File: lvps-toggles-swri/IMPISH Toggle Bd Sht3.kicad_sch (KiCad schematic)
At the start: 66 parts, among them J3 BCS-110-L-D-TE, J4 BCS-110-L-D-TE, Q1 MMBT3904Q, Q10 MMBT3904Q, Q11 MMBT3906Q, Q12 ZXM61N02F, Q2 MMBT3906Q, Q3 ZXM61N02F, Q4 MMBT3904Q, Q5 MMBT3906Q, Q6 ZXM61N02F, Q7 MMBT3904Q, Q8 MMBT3906Q, Q9 ZXM61N02F, U1 BSP452, U2 AP22804AW5-7, U3 AP22804AW5-7, U4 BSP452, U5 AP22804AW5-7, U6 AP22804AW5-7

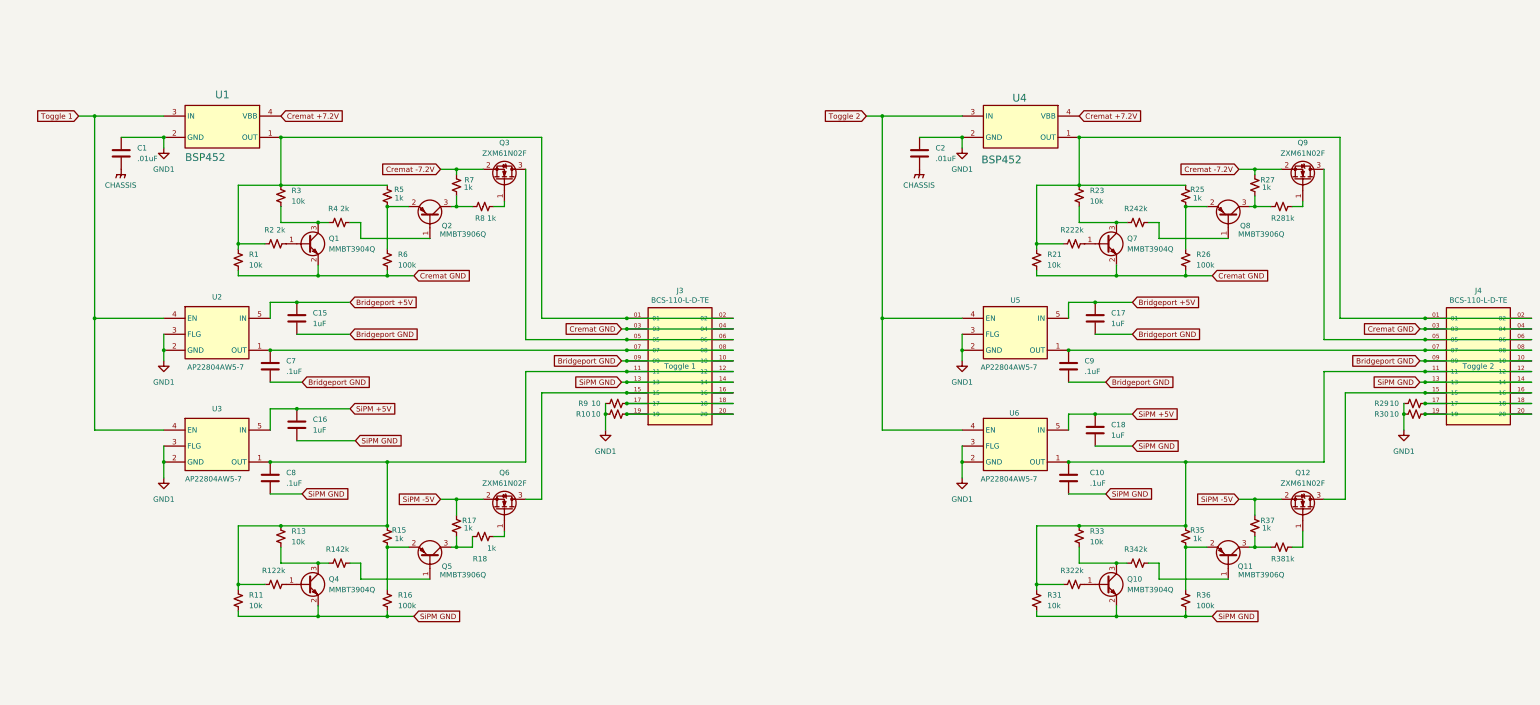
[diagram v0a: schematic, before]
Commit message: Power board updates (#7)
* toggles adapter board

The SwRI toggle output is in the wrong direction,
so we are adding an additional PCB to point the power
towards the side of the EPS box. We can route it with
cables and connectors instead of using the board-to-board
style interface.

* toggles adapter: cleanup

* toggles adapter: via stitching

* swri toggles: start one ground

* swri toggles: single ground pre stitching

* swri toggles: via stitching for gnd

* swri toggles: fix DRC and ERC errors

* swri lvps main: two layer board

* swri lvps main: fix cap models
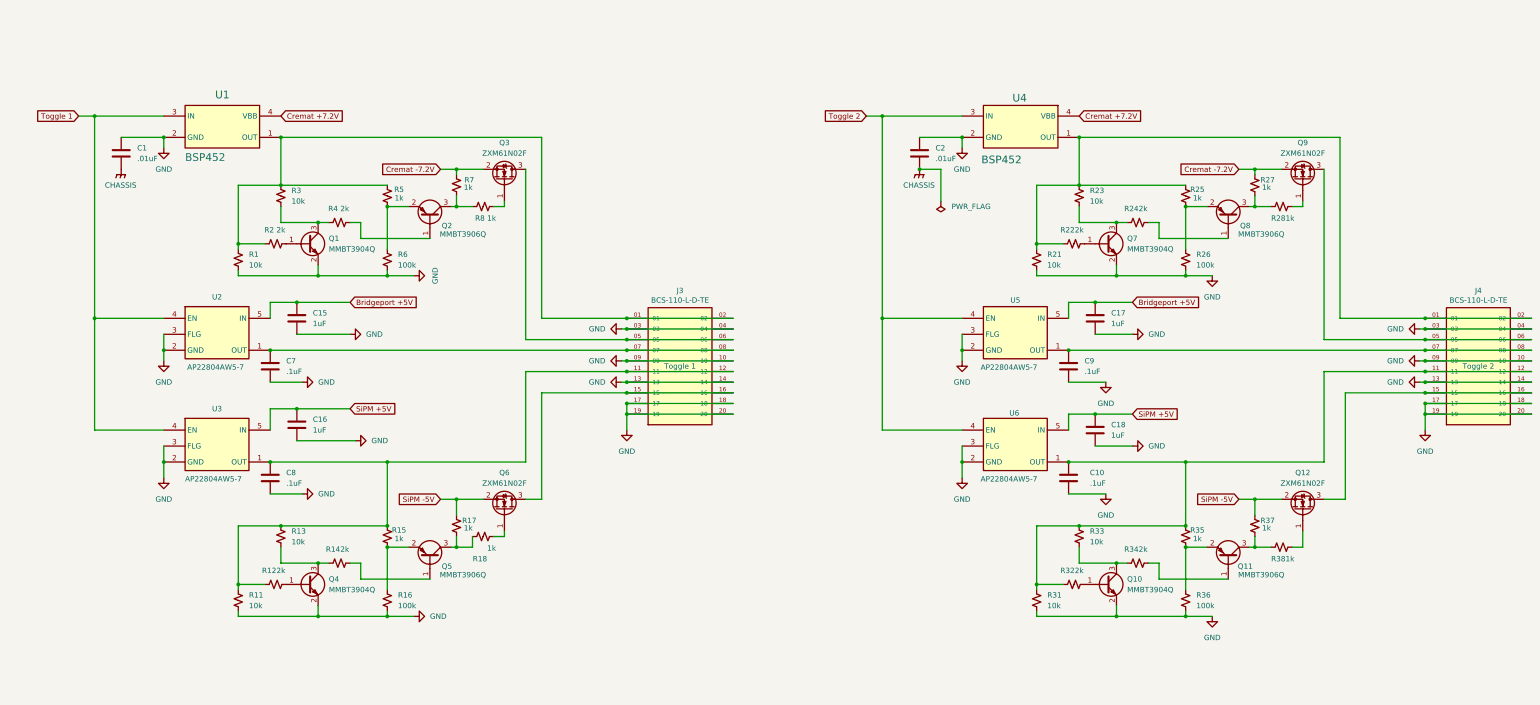
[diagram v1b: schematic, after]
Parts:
- removed R10, R29, R30, R9: 10, Resistor_SMD:R_0805_2012Metric_Pad1.20x1.40mm_HandSolder, symbol Device:R_Small_US
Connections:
- net Bridgeport GND is gone; now on net GND: C15.2, C17.2, C7.2, C9.2, J3.09, J3.10, J4.09, J4.10
- net Cremat GND is gone; now on net GND: J3.03, J3.04, J4.03, J4.04, Q1.2 (E), Q7.2 (E), R1.2, R21.2, R26.2, R6.2
- net GND1 is gone; now on net GND: C1.1, C2.2, U1.2 (GND), U2.2 (GND), U2.3 (FLG), U3.2 (GND), U3.3 (FLG), U4.2 (GND), U5.2 (GND), U5.3 (FLG), U6.2 (GND), U6.3 (FLG)
- net SiPM GND is gone; now on net GND: C10.2, C16.2, C18.2, C8.2, J3.13, J3.14, J4.13, J4.14, Q10.2 (E), Q4.2 (E), R11.2, R16.2, R31.2, R36.2
- net GND: now reaches J4.17, J4.18
- net GND: now also J3.17, J3.18, J3.19, J3.20, J4.19, J4.20

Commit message: toggles
remove cremat, fix layout, add DAQBOX toggle/power line
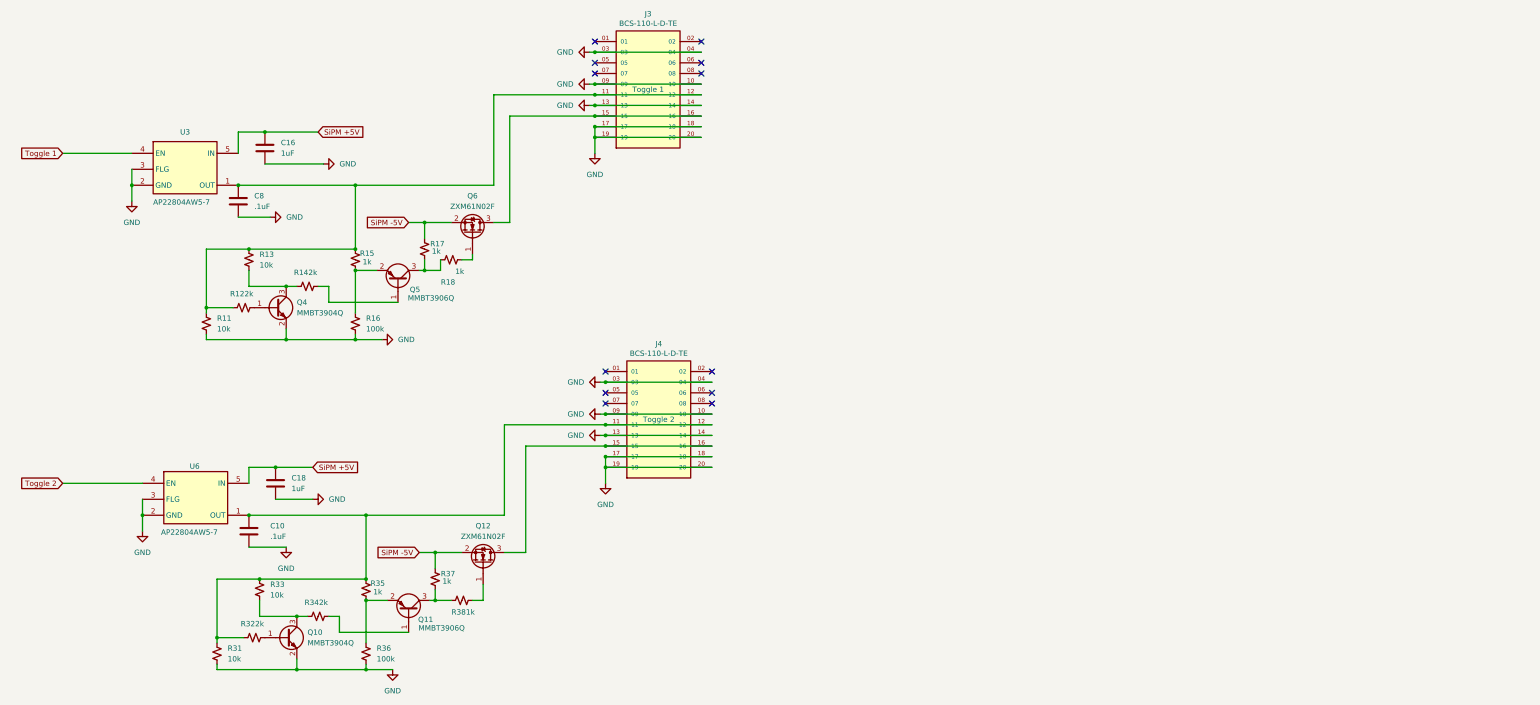
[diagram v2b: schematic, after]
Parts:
- removed C1, C2: .01uF, Capacitor_SMD:C_0805_2012Metric_Pad1.18x1.45mm_HandSolder, symbol IMPISH Toggles Library:.01uF
- removed C15, C17: 1uF, Capacitor_SMD:C_0805_2012Metric_Pad1.18x1.45mm_HandSolder, symbol IMPISH Toggles Library:1uF
- removed C7, C9: .1uF, Capacitor_SMD:C_0805_2012Metric_Pad1.18x1.45mm_HandSolder, symbol IMPISH Toggles Library:.1uF
- removed Q1, Q7: MMBT3904Q, Package_TO_SOT_SMD:SOT-23, symbol Transistor_BJT:MMBT3904
- removed Q2, Q8: MMBT3906Q, Package_TO_SOT_SMD:SOT-23, symbol Transistor_BJT:MMBT3906
- removed Q3, Q9: ZXM61N02F, Package_TO_SOT_SMD:SOT-23, symbol IMPISH Toggles Library:ZXM61N02F
- removed R1, R21, R23, R3: 10k, Resistor_SMD:R_0805_2012Metric_Pad1.20x1.40mm_HandSolder, symbol Device:R_Small_US
- removed R2, R22, R24, R4: 2k, Resistor_SMD:R_0805_2012Metric_Pad1.20x1.40mm_HandSolder, symbol Device:R_Small_US
- removed R25, R27, R28, R5, R7, R8: 1k, Resistor_SMD:R_0805_2012Metric_Pad1.20x1.40mm_HandSolder, symbol Device:R_Small_US
- removed R26, R6: 100k, Resistor_SMD:R_0805_2012Metric_Pad1.20x1.40mm_HandSolder, symbol Device:R_Small_US
- removed U1, U4: BSP452, IMPISH Toggles Library:SOT230P700X180-4N-3-V, symbol IMPISH Toggles Library:BSP452
- removed U2, U5: AP22804AW5-7, IMPISH Toggles Library:SOT95P285X140-5N, symbol IMPISH Toggles Library:AP22804AW5-7
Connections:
- net at J3.01: no longer J3.02
- net at J4.01: no longer J4.02
- net at J4.07: no longer J4.08
- net at J3.05: no longer J3.06
- net at J3.07: no longer J3.08
- net at J4.05: no longer J4.06
- no-connect marks 0 -> 12
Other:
- moved on the sheet: C10, C16, C18, C8, J3, J4, Q10, Q11, Q12, Q4, Q5, Q6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
